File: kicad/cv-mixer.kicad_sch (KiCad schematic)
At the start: 20 parts, among them J15 Eurorack Mono Jack, J16 Eurorack Mono Jack, J17 Eurorack Mono Jack, J18 Eurorack Mono Jack, U2 TL072

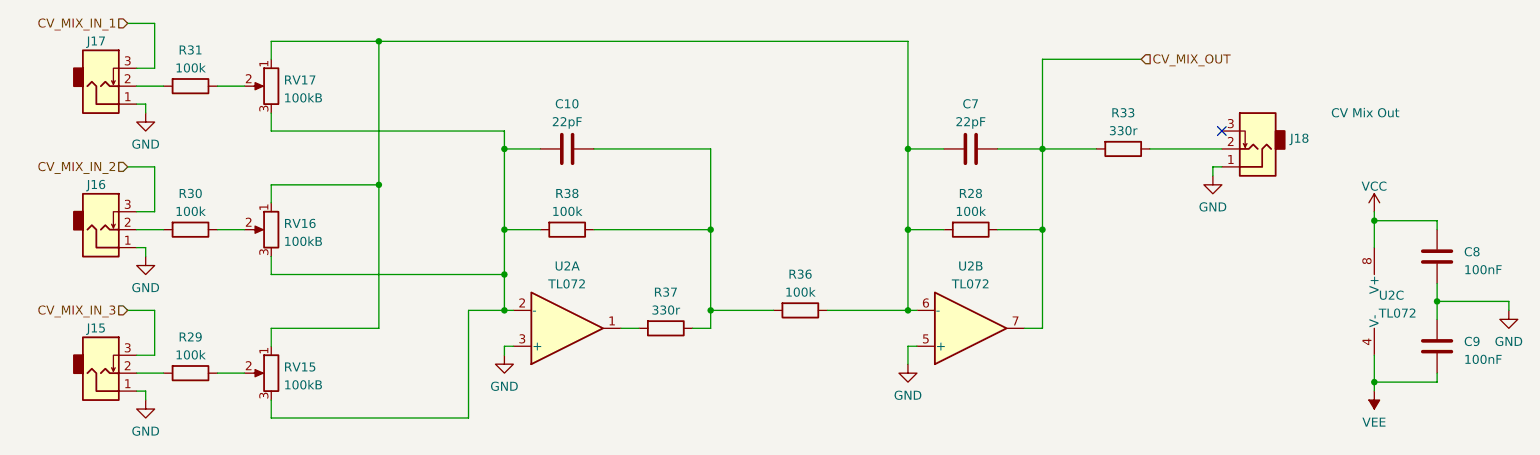
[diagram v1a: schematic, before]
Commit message: Updating board for new footprint libraries
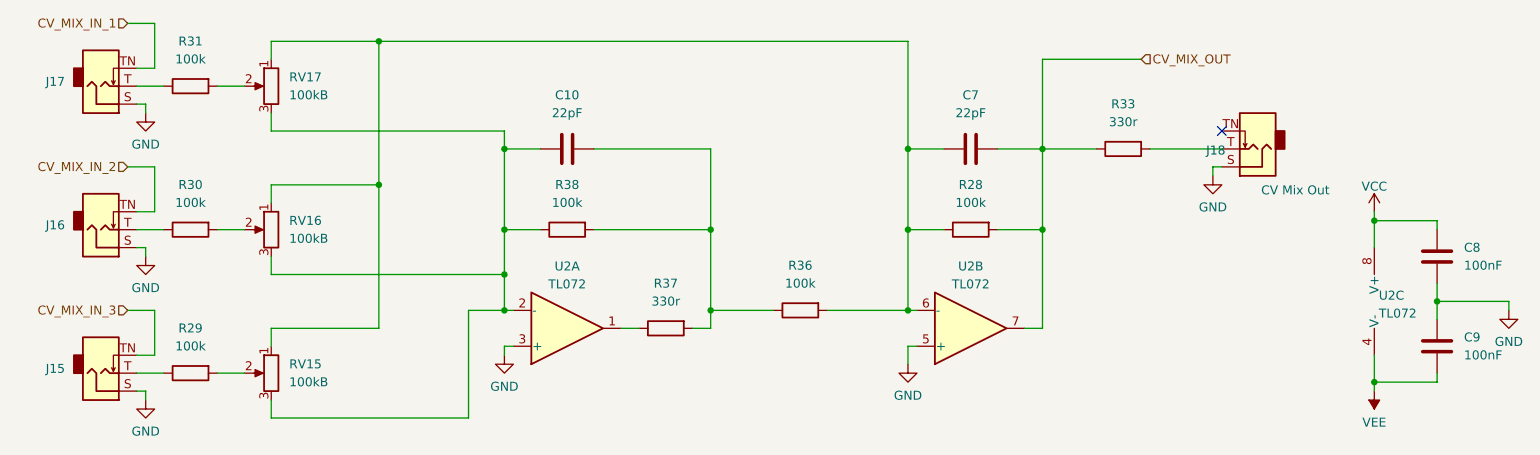
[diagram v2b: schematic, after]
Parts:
- C10, C7, C8, C9: symbol Rumblesan Standard Parts:C -> Rumblesan_Standard_Parts:C
- J15, J16, J17, J18: footprint Rumblesan_Standard_Parts:Jack_3.5mm_QingPu_WQP-PJ398SM_Vertical -> Rumblesan_Audio_Connectors:Jack_3.5mm_QingPu_WQP-PJ398SM_Vertical; symbol Audio_Connectors:Eurorack_Mono_Jack -> Connector_Audio:AudioJack2_SwitchT
- R28, R29, R30, R31, R33, R36, R37, R38: symbol Rumblesan Standard Parts:R -> Rumblesan_Standard_Parts:R
- RV15, RV16, RV17: footprint Rumblesan_Standard_Parts:Potentiometer_Alpha_RD901F-40-00D_Single_Vertical -> Rumblesan_Potentiometer_THT:Potentiometer_Alpha_RD901F-40-00D_Single_Vertical; symbol Rumblesan Standard Parts:R_Potentiometer -> Rumblesan_Standard_Parts:R_Potentiometer
- U2: footprint Rumblesan_Standard_Parts:DIP-8_W7.62mm_Socket -> Package_DIP:DIP-8_W7.62mm_Socket
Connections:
- net CV_MIX_IN_1: now also J17.TN; no longer J17.3 (Tip_normalize)
- net CV_MIX_IN_2: now also J16.TN; no longer J16.3 (Tip_normalize)
- net CV_MIX_IN_3: now also J15.TN; no longer J15.3 (Tip_normalize)
- net GND: now also J15.S, J16.S, J17.S, J18.S; no longer J15.1 (Sleeve), J16.1 (Sleeve), J17.1 (Sleeve), J18.1 (Sleeve)
- net at R31.2: now also J17.T; no longer J17.2 (Tip)
- net at R30.2: now also J16.T; no longer J16.2 (Tip)
- net at R33.1: now also J18.T; no longer J18.2 (Tip)
- net at R29.2: now also J15.T; no longer J15.2 (Tip)
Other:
- moved on the sheet: J18, R28, R29, R30, R31, R33, R36, R37, R38

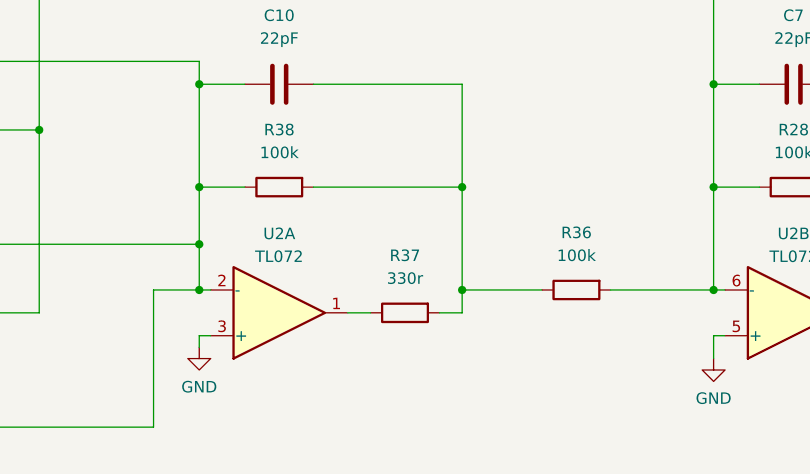
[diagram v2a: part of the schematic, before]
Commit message: Updating with rev03 changes
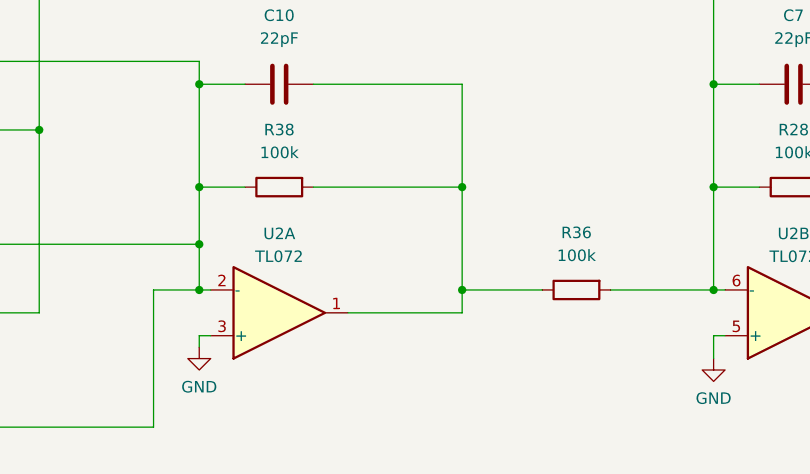
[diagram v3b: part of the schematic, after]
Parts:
- removed R37: 330r, Rumblesan_Standard_Parts:R_Axial_DIN0207_L6.3mm_D2.5mm_P10.16mm_Horizontal, symbol Rumblesan_Standard_Parts:R
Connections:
- net at C10.2, R36.2, R38.1: now also U2.1
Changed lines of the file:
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@@
 (kicad_sch
-	(version 20231120)
+	(version 20250114)
 	(generator "eeschema")
-	(generator_version "8.0")
+	(generator_version "9.0")
 	(paper "A4")
 	(title_block
@@
 	(wire
 		(pts
-			(xy 115.57 90.17) (xy 118.11 90.17)
+			(xy 115.57 90.17) (xy 128.27 90.17)
 		)
 		(stroke
@@
 		(pts
 			(xy 93.98 102.87) (xy 93.98 87.63)
-		)
-		(stroke
-			(width 0)
-			(type default)
-		)
-	)
-	(wire
-		(pts
-			(xy 125.73 90.17) (xy 128.27 90.17)
 		)
 		(stroke
@@
 		(shape input)
 		(at 45.72 67.31 180)
-		(fields_autoplaced yes)
 		(effects
 			(font
@@
 		(shape input)
 		(at 45.72 46.99 180)
-		(fields_autoplaced yes)
 		(effects
 			(font
@@
 		(shape input)
 		(at 189.23 52.07 0)
-		(fields_autoplaced yes)
 		(effects
 			(font
@@
 		(shape input)
 		(at 45.72 87.63 180)
-		(fields_autoplaced yes)
 		(effects
 			(font
@@
 					(unit 1)
 				)
-			)
-		)
-	)
-	(symbol
-		(lib_id "Rumblesan_Standard_Parts:R")
-		(at 121.92 90.17 270)
-		(unit 1)
-		(exclude_from_sim no)
-		(in_bom yes)
-		(on_board yes)
-		(dnp no)
-		(fields_autoplaced yes)
-		(property "Reference" "R37"
-			(at 121.92 83.82 90)
-			(effects
-				(font
-					(size 1.27 1.27)
-				)
-			)
-		)
-		(property "Value" "330r"
-			(at 121.92 86.36 90)
-			(effects
-				(font
-					(size 1.27 1.27)
-				)
-			)
-		)
-		(property "Footprint" "Rumblesan_Standard_Parts:R_Axial_DIN0207_L6.3mm_D2.5mm_P10.16mm_Horizontal"
-			(at 119.38 92.71 90)
-			(effects
-				(font
-					(size 1.27 1.27)
-				)
-				(hide yes)
-			)
-		)
-		(property "Datasheet" "~"
-			(at 121.92 96.52 90)
-			(effects
-				(font
-					(size 1.27 1.27)
-				)
-				(hide yes)
-			)
-		)
-		(property "Description" "Resistor"
-			(at 121.92 90.17 0)
-			(effects
-				(font
-					(size 1.27 1.27)
-				)
-				(hide yes)
-			)
-		)
-		(property "Tolerance" "1%"
-			(at 115.57 95.25 90)
-			(effects
-				(font
-					(size 1.27 1.27)
-				)
-				(hide yes)
-			)
-		)
-		(property "Power" "0.5W"
-			(at 129.54 95.25 90)
-			(effects
-				(font
-					(size 1.27 1.27)
-				)
-				(hide yes)
-			)
-		)
-		(property "Spec" "metal film"
-			(at 121.92 95.25 90)
-			(effects
-				(font
-					(size 1.27 1.27)
-				)
-				(hide yes)
-			)
-		)
-		(pin "1"
-		)
-		(pin "2"
-		)
-		(instances
-			(project "ouroboros"
-				(path "/5b0acaca-dc50-4fa5-b146-164c1b9ad031/8910ec24-817d-4de5-97c2-6d5a7027c76c"
-					(reference "R37")
-					(unit 1)
-				)
